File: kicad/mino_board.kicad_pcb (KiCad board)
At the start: 2 copper layers, 224.8 x 91.4 mm, 39 parts, among them J1-2 Conn_01x04, J10 Conn_01x04, J2 Conn_01x05, J4 Conn_02x10_Counter_Clockwise, P1 LED, P2 LED, P3 LED, P4 LED, X1 SW_Push, Y1 SW_Push

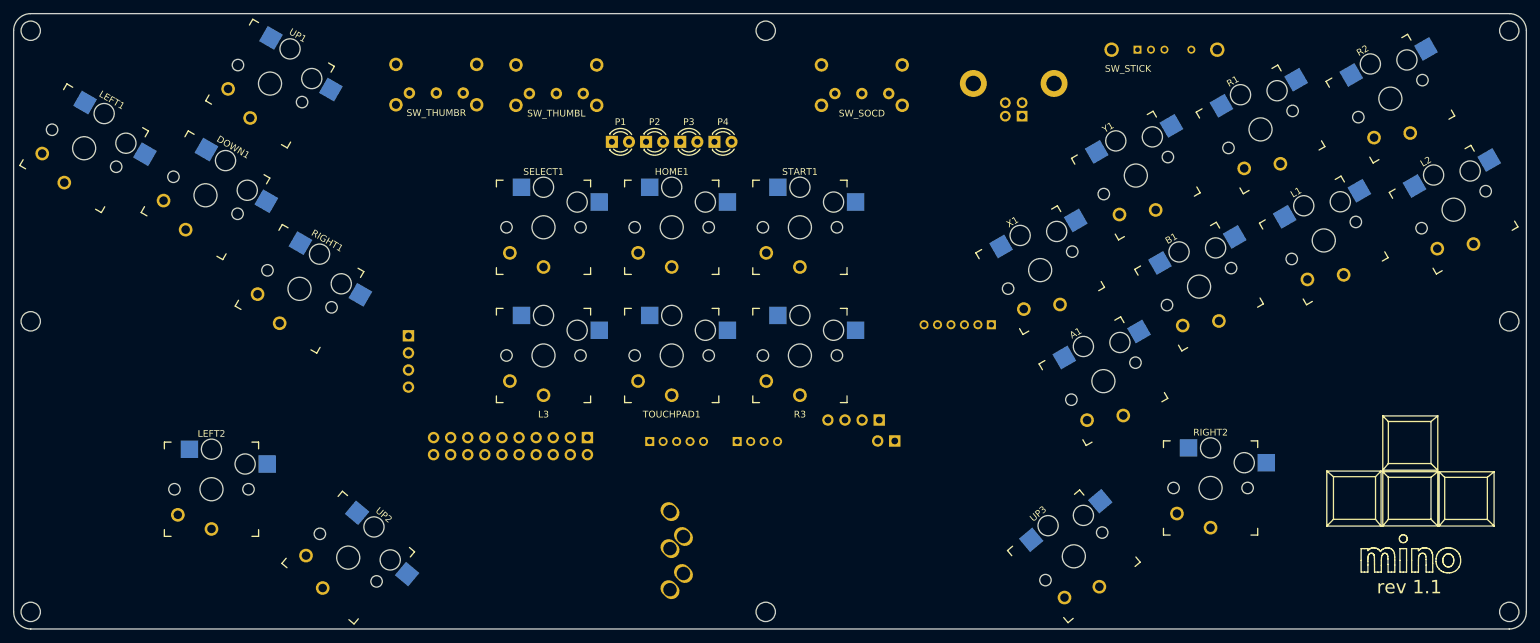
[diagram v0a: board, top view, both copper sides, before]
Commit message: Dip Switches
Swap out the toggle switches for dip switches to control the spare thumb buttons.
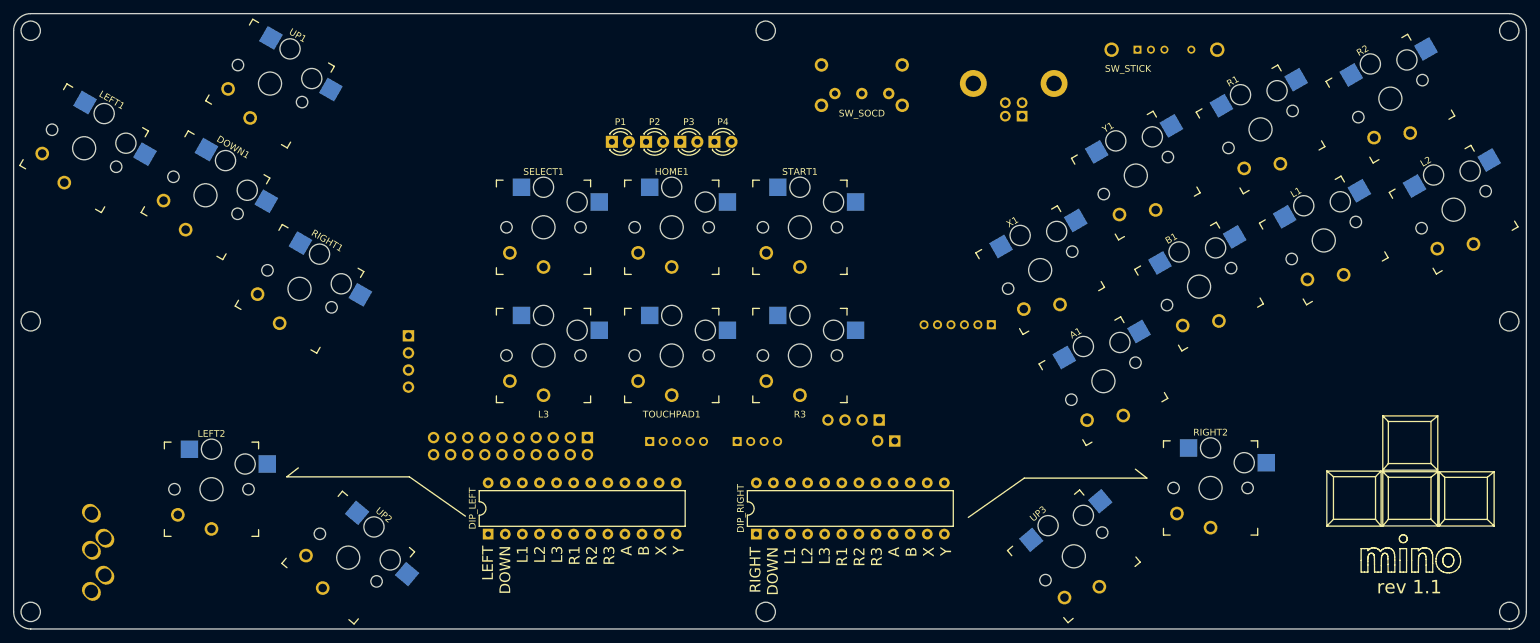
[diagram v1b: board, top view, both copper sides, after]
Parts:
- removed SW_THUMBL, SW_THUMBR: SW_E-Switch_EG1224_SPDT_Angled, Button_Switch_THT:SW_E-Switch_EG1224_SPDT_Angled
- added DIP_LEFT: DIP-24_W7.62mm, Package_DIP:DIP-24_W7.62mm, F.Cu at (118.8, 142.1)
- added DIP_RIGHT: DIP-24_W7.62mm, Package_DIP:DIP-24_W7.62mm, F.Cu at (158.6, 142.1)
- moved AUDIO 86.0 mm to (59.8, 150.6)
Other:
- board text added: "LEFT DOWN L1 L2 L3 R1 R2 R3 A B X Y"
- board text added: "RIGHT DOWN L1 L2 L3 R1 R2 R3 A B X Y"

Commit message: Remove Audio Jack
Remove the audio jack until I can figure out how it works
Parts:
- removed AUDIO: Jack_3.5mm_CUI_SJ1-3535NG_Horizontal_CircularHoles, Connector_Audio:Jack_3.5mm_CUI_SJ1-3535NG_Horizontal_CircularHoles
- removed JAUDIO: PinHeader_1x06_P2.00mm_Vertical, Connector_PinHeader_2.00mm:PinHeader_1x06_P2.00mm_Vertical

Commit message: Route the new board
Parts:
- DIP_LEFT1: renamed from DIP_LEFT; value DIP-24_W7.62mm -> DIP_LEFT
- DIP_RIGHT1: renamed from DIP_RIGHT; value DIP-24_W7.62mm -> DIP_RIGHT
- JSOCD1: renamed from JSOCD; value PinHeader_1x02_P2.54mm_Vertical -> Conn_01x02
- JSTICKTYPE1: renamed from JSTICKTYPE; value PinHeader_1x04_P2.54mm_Vertical -> Conn_01x04
- SW_SOCD1: renamed from SW_SOCD; value SW_E-Switch_EG1224_SPDT_Angled -> SW_SPDT
- SW_STICK1: renamed from SW_STICK; value (none) -> SW_SP3T
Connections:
- DIP_LEFT1 pad 1: (no net) -> Net-(DIP_LEFT1-Pad1)
- DIP_LEFT1 pad 10: (no net) -> Net-(B1-Pad1)
- DIP_LEFT1 pad 11: (no net) -> Net-(DIP_LEFT1-Pad11)
- DIP_LEFT1 pad 12: (no net) -> Net-(DIP_LEFT1-Pad12)
- DIP_LEFT1 pad 13: (no net) -> Net-(DIP_LEFT1-Pad13)
- DIP_LEFT1 pad 14: (no net) -> Net-(DIP_LEFT1-Pad13)
- DIP_LEFT1 pad 15: (no net) -> Net-(DIP_LEFT1-Pad13)
- DIP_LEFT1 pad 16: (no net) -> Net-(DIP_LEFT1-Pad13)
- DIP_LEFT1 pad 17: (no net) -> Net-(DIP_LEFT1-Pad13)
- DIP_LEFT1 pad 18: (no net) -> Net-(DIP_LEFT1-Pad13)
- DIP_LEFT1 pad 19: (no net) -> Net-(DIP_LEFT1-Pad13)
- DIP_LEFT1 pad 2: (no net) -> Net-(DIP_LEFT1-Pad2)
- DIP_LEFT1 pad 20: (no net) -> Net-(DIP_LEFT1-Pad13)
- DIP_LEFT1 pad 21: (no net) -> Net-(DIP_LEFT1-Pad13)
- DIP_LEFT1 pad 22: (no net) -> Net-(DIP_LEFT1-Pad13)
- DIP_LEFT1 pad 23: (no net) -> Net-(DIP_LEFT1-Pad13)
- DIP_LEFT1 pad 24: (no net) -> Net-(DIP_LEFT1-Pad13)
- DIP_LEFT1 pad 3: (no net) -> Net-(DIP_LEFT1-Pad3)
- DIP_LEFT1 pad 4: (no net) -> Net-(DIP_LEFT1-Pad4)
- DIP_LEFT1 pad 5: (no net) -> Net-(DIP_LEFT1-Pad5)
- DIP_LEFT1 pad 6: (no net) -> Net-(DIP_LEFT1-Pad6)
- DIP_LEFT1 pad 7: (no net) -> Net-(DIP_LEFT1-Pad7)
- DIP_LEFT1 pad 8: (no net) -> Net-(DIP_LEFT1-Pad8)
- DIP_LEFT1 pad 9: (no net) -> Net-(A1-Pad1)
- DIP_RIGHT1 pad 1: (no net) -> Net-(DIP_RIGHT1-Pad1)
- DIP_RIGHT1 pad 10: (no net) -> Net-(B1-Pad1)
- DIP_RIGHT1 pad 11: (no net) -> Net-(DIP_LEFT1-Pad11)
- DIP_RIGHT1 pad 12: (no net) -> Net-(DIP_LEFT1-Pad12)
- DIP_RIGHT1 pad 13: (no net) -> Net-(DIP_RIGHT1-Pad13)
- DIP_RIGHT1 pad 14: (no net) -> Net-(DIP_RIGHT1-Pad13)
- DIP_RIGHT1 pad 15: (no net) -> Net-(DIP_RIGHT1-Pad13)
- DIP_RIGHT1 pad 16: (no net) -> Net-(DIP_RIGHT1-Pad13)
- DIP_RIGHT1 pad 17: (no net) -> Net-(DIP_RIGHT1-Pad13)
- DIP_RIGHT1 pad 18: (no net) -> Net-(DIP_RIGHT1-Pad13)
- DIP_RIGHT1 pad 19: (no net) -> Net-(DIP_RIGHT1-Pad13)
- DIP_RIGHT1 pad 2: (no net) -> Net-(DIP_LEFT1-Pad2)
- DIP_RIGHT1 pad 20: (no net) -> Net-(DIP_RIGHT1-Pad13)
- DIP_RIGHT1 pad 21: (no net) -> Net-(DIP_RIGHT1-Pad13)
- DIP_RIGHT1 pad 22: (no net) -> Net-(DIP_RIGHT1-Pad13)
- DIP_RIGHT1 pad 23: (no net) -> Net-(DIP_RIGHT1-Pad13)
- DIP_RIGHT1 pad 24: (no net) -> Net-(DIP_RIGHT1-Pad13)
- DIP_RIGHT1 pad 3: (no net) -> Net-(DIP_LEFT1-Pad3)
- DIP_RIGHT1 pad 4: (no net) -> Net-(DIP_LEFT1-Pad4)
- DIP_RIGHT1 pad 5: (no net) -> Net-(DIP_LEFT1-Pad5)
- DIP_RIGHT1 pad 6: (no net) -> Net-(DIP_LEFT1-Pad6)
- DIP_RIGHT1 pad 7: (no net) -> Net-(DIP_LEFT1-Pad7)
- DIP_RIGHT1 pad 8: (no net) -> Net-(DIP_LEFT1-Pad8)
- DIP_RIGHT1 pad 9: (no net) -> Net-(A1-Pad1)
- DOWN1 pad 1: Net-(DOWN1-Pad1) -> Net-(DIP_LEFT1-Pad2)
- J10 pad 2: Net-(J10-Pad2) -> Net-(DIP_LEFT1-Pad5)
- J10 pad 3: Net-(J10-Pad3) -> Net-(DIP_LEFT1-Pad8)
- J4 pad 10: Net-(J4-Pad10) -> Net-(DIP_LEFT1-Pad6)
- J4 pad 11: Net-(J4-Pad11) -> Net-(DIP_LEFT1-Pad3)
- J4 pad 15: Net-(J4-Pad15) -> Net-(DIP_LEFT1-Pad7)
- J4 pad 16: Net-(J4-Pad16) -> Net-(DIP_LEFT1-Pad4)
- J4 pad 2: Net-(DOWN1-Pad1) -> Net-(DIP_LEFT1-Pad2)
- J4 pad 3: Net-(J4-Pad3) -> Net-(DIP_RIGHT1-Pad1)
- J4 pad 4: Net-(J4-Pad4) -> Net-(DIP_LEFT1-Pad1)
- J4 pad 8: Net-(J4-Pad8) -> Net-(DIP_LEFT1-Pad11)
- J4 pad 9: Net-(J4-Pad9) -> Net-(DIP_LEFT1-Pad12)
- JSOCD1 pad 1: (no net) -> Net-(JSOCD1-Pad1)
- JSOCD1 pad 2: (no net) -> Net-(JSOCD1-Pad2)
- JSTICKTYPE1 pad 1: (no net) -> Net-(JSTICKTYPE1-Pad1)
- JSTICKTYPE1 pad 2: (no net) -> Net-(JSTICKTYPE1-Pad2)
- JSTICKTYPE1 pad 3: (no net) -> Net-(JSTICKTYPE1-Pad3)
- JSTICKTYPE1 pad 4: (no net) -> Net-(JSTICKTYPE1-Pad4)
- L1 pad 1: Net-(J4-Pad11) -> Net-(DIP_LEFT1-Pad3)
- L2 pad 1: Net-(J4-Pad16) -> Net-(DIP_LEFT1-Pad4)
- L3 pad 1: Net-(J10-Pad2) -> Net-(DIP_LEFT1-Pad5)
- LEFT1 pad 1: Net-(J4-Pad4) -> Net-(DIP_LEFT1-Pad1)
- LEFT2 pad 1: Net-(J4-Pad4) -> Net-(DIP_LEFT1-Pad13)
- R1 pad 1: Net-(J4-Pad10) -> Net-(DIP_LEFT1-Pad6)
- R2 pad 1: Net-(J4-Pad15) -> Net-(DIP_LEFT1-Pad7)
- R3 pad 1: Net-(J10-Pad3) -> Net-(DIP_LEFT1-Pad8)
- RIGHT1 pad 1: Net-(J4-Pad3) -> Net-(DIP_RIGHT1-Pad1)
- RIGHT2 pad 1: Net-(J4-Pad3) -> Net-(DIP_RIGHT1-Pad13)
- SW_SOCD1 pad 1: (no net) -> Net-(JSOCD1-Pad1)
- SW_SOCD1 pad 2: (no net) -> Net-(JSOCD1-Pad2)
- SW_SOCD1 pad 3: (no net) -> Net-(SW_SOCD1-Pad3)
- SW_STICK1 pad 1: (no net) -> Net-(JSTICKTYPE1-Pad1)
- SW_STICK1 pad 2: (no net) -> Net-(JSTICKTYPE1-Pad3)
- SW_STICK1 pad 3: (no net) -> Net-(JSTICKTYPE1-Pad2)
- SW_STICK1 pad 4: (no net) -> Net-(JSTICKTYPE1-Pad4)
- X1 pad 1: Net-(J4-Pad8) -> Net-(DIP_LEFT1-Pad11)
- Y1 pad 1: Net-(J4-Pad9) -> Net-(DIP_LEFT1-Pad12)
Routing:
- net Net-(A1-Pad2): track 0.00 -> 661.0 mm
- net Net-(J4-Pad1): track 0.00 -> 213.8 mm, vias 0 -> 2
- net Net-(DIP_LEFT1-Pad7): track 0.00 -> 209.7 mm
- net Net-(DIP_LEFT1-Pad4): track 0.00 -> 197.5 mm
- net Net-(DIP_LEFT1-Pad3): track 0.00 -> 172.3 mm
- net Net-(DIP_LEFT1-Pad6): track 0.00 -> 167.0 mm
- net Net-(DIP_LEFT1-Pad2): track 0.00 -> 153.2 mm
- net Net-(B1-Pad1): track 0.00 -> 150.4 mm
- net Net-(DIP_LEFT1-Pad12): track 0.00 -> 148.5 mm
- net Net-(JSTICKTYPE1-Pad4): track 0.00 -> 144.5 mm
- net Net-(A1-Pad1): track 0.00 -> 137.9 mm, vias 0 -> 2
- net Net-(JSTICKTYPE1-Pad2): track 0.00 -> 137.9 mm
- net Net-(JSTICKTYPE1-Pad3): track 0.00 -> 132.8 mm
- net Net-(JSTICKTYPE1-Pad1): track 0.00 -> 125.9 mm
- net Net-(DIP_LEFT1-Pad1): track 0.00 -> 123.6 mm
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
